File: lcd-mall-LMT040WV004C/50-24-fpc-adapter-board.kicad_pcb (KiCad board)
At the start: 4 copper layers, 28.8 x 25.2 mm, 19 parts, among them J1 1-1734248-5, J2 FFC2B35-24-G, SW1 SMD-BUTTON_4P-5.2X5.2X1.5MM-S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, U1 RS3236-1.8FY5, U3 AP3127B

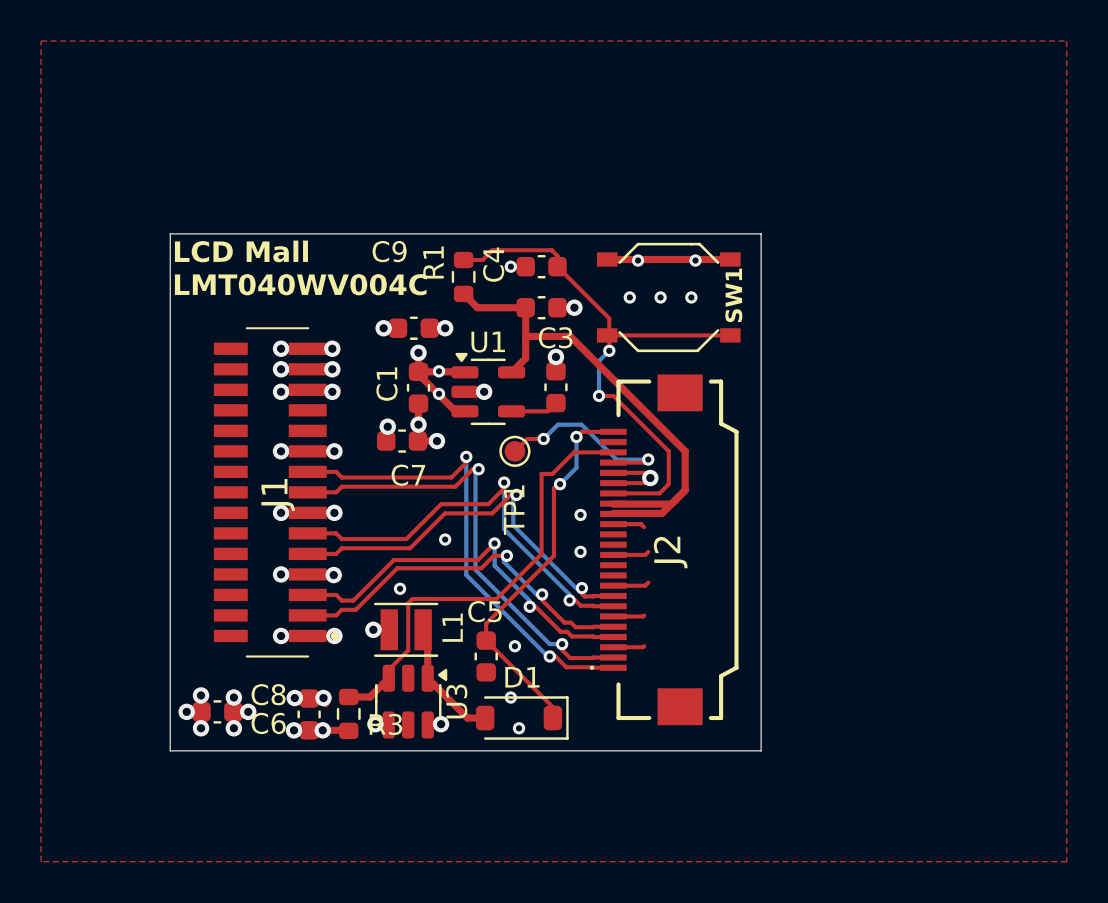
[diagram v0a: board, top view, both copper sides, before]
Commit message: Fix names, footprints, and silkscreen of the pcb's
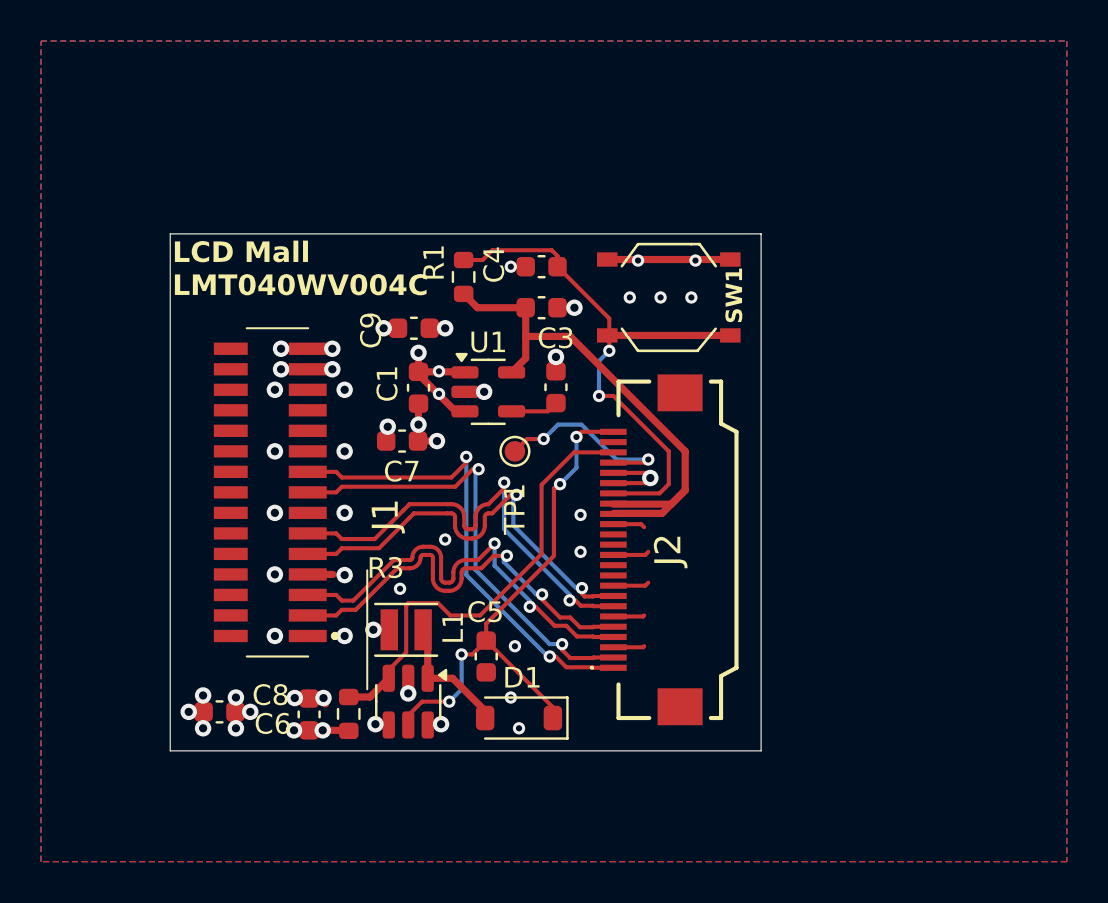
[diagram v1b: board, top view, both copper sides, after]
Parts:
- moved C8 0.10 mm to (68.7, 72.7)
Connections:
- U3 pad 5: (no net) -> LEDA
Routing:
- net GND: track 38.4 -> 27.2 mm, vias 34 -> 35
- net LEDA: track 18.8 -> 25.6 mm, vias 2 -> 4
- net D1_P: track 18.9 -> 21.3 mm
- net D1_N: track 18.1 -> 20.6 mm
- net CLK_C_P: track 20.3 -> 22.0 mm
- net CLK_C_N: track 19.4 -> 21.1 mm
- added copper zone on B.Cu, net GND

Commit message: Fix parts for board LMT040WM004C
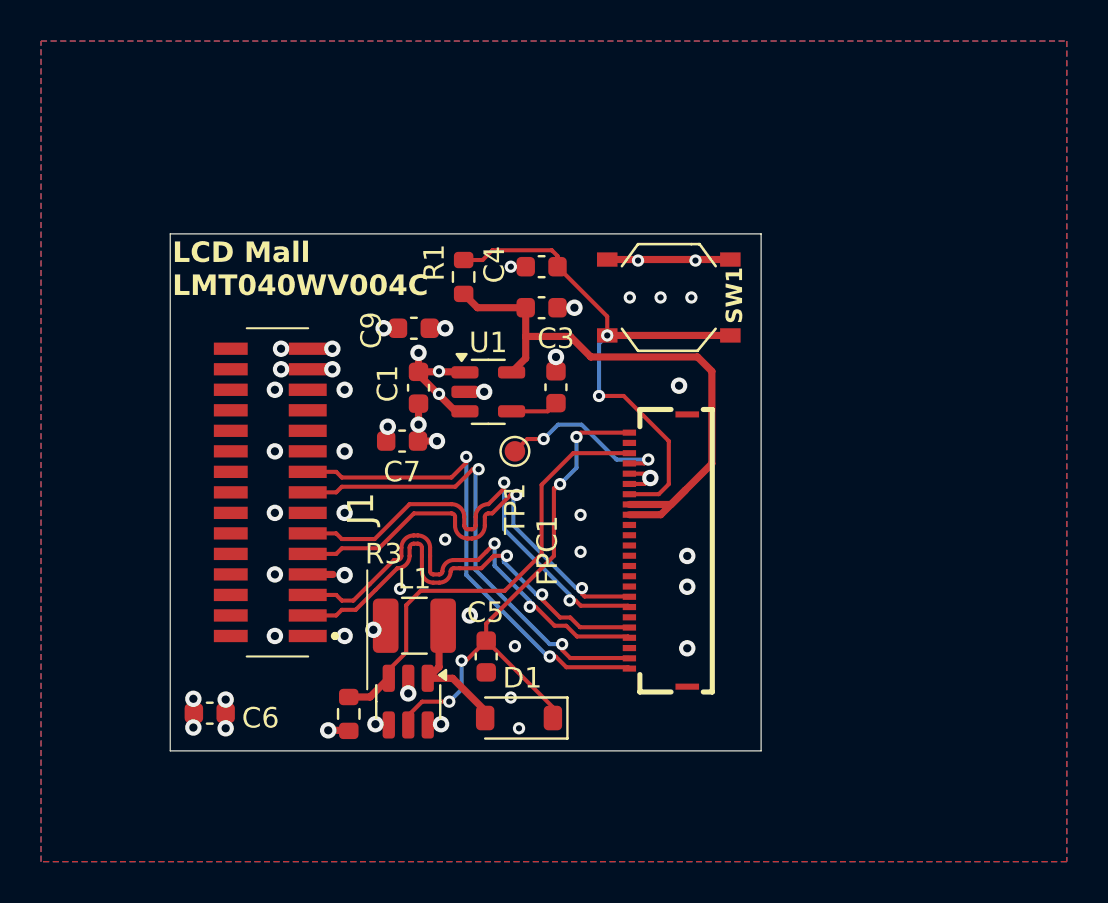
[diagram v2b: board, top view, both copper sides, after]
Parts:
- removed C8: 10nF, Capacitor_SMD:C_0603_1608Metric
- removed J2: FFC2B35-24-G, custom:FFC2B3524G
- added FPC1: 0.5K-QX-24PWB, easyeda2kicad:FPC-SMD_24P-P0.50_HDGC_0.5K-QX-24PWB, F.Cu at (90.1, 64.8)
- L1: value 22uH -> 6.8uH; footprint Inductor_SMD:L_Changjiang_FNR252010S -> Inductor_SMD:L_1210_3225Metric
- R3: value 6R2 1% -> 10R0 1%
- U3: value AP3127B -> AP3032
- moved C6 4.84 mm to (68.2, 72.8), turned to 0 degrees
- moved L1 0.45 mm to (78.2, 68.5)
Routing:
- net GND: track 27.2 -> 16.5 mm, vias 35 -> 38
- net +3V3: track 22.3 -> 17.3 mm, vias 18 -> 15
- net +1V8: track 26.5 -> 29.1 mm
- net D1_P: track 21.3 -> 22.4 mm
- net D1_N: track 20.6 -> 21.6 mm
- net CLK_C_P: track 22.0 -> 22.8 mm
- net D0_P: track 23.2 -> 24.0 mm
- net D0_N: track 22.4 -> 23.2 mm
- net CLK_C_N: track 21.1 -> 21.9 mm
- net Net-(FPC1-Pad21): track 9.50 -> 8.74 mm
- net RST: track 28.0 -> 27.4 mm
